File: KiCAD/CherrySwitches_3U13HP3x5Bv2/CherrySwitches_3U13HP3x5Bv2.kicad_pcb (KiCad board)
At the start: 2 copper layers, 65.7 x 128.5 mm, 19 parts

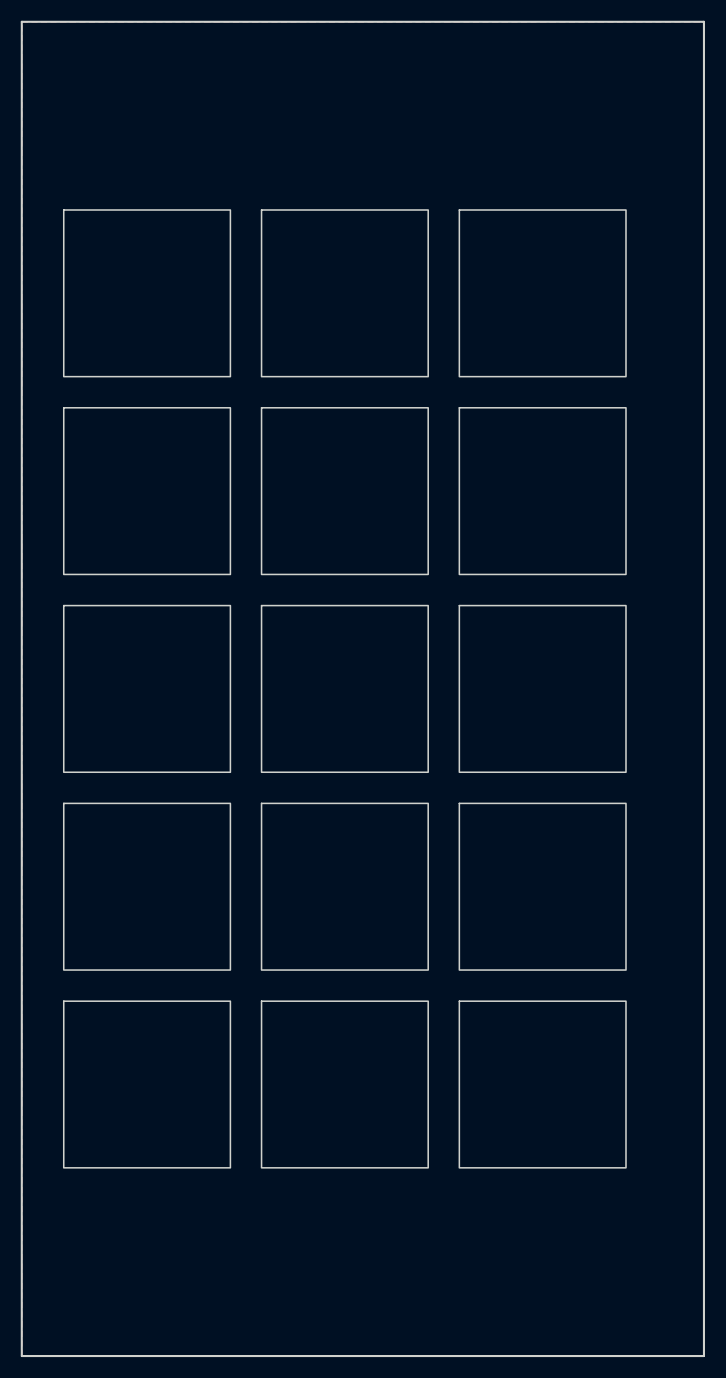
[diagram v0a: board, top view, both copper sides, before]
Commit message: updated all modules to use plated through-holes wherever possible
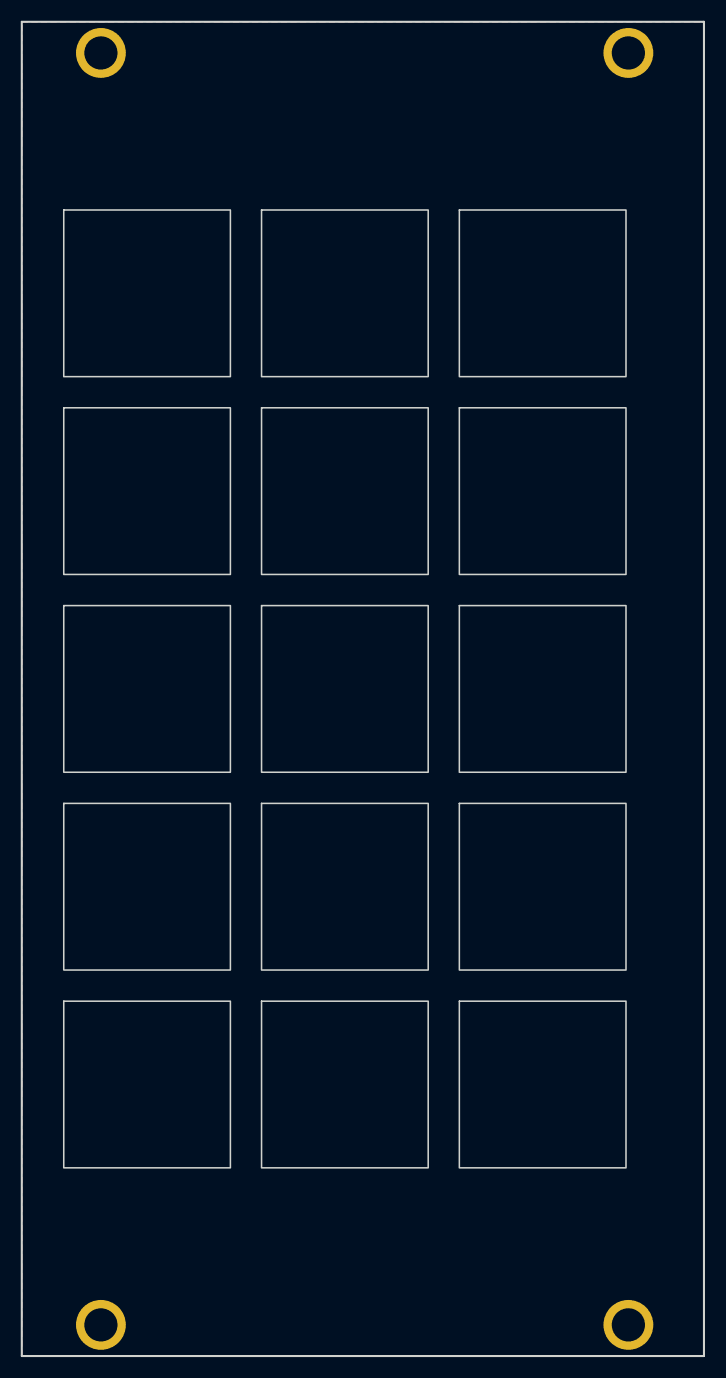
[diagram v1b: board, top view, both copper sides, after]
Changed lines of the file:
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@@
 			)
 		)
-		(pad "" np_thru_hole oval
+		(pad "" thru_hole circle
 			(at 0 0)
-			(size 4.34 3.2)
-			(drill oval 4.34 3.2)
+			(size 4.8 4.8)
+			(drill 3.2)
 			(layers "*.Cu" "*.Mask")
+			(remove_unused_layers no)
 		)
 		(embedded_fonts no)
@@
 			)
 		)
-		(pad "" np_thru_hole oval
+		(pad "" thru_hole circle
 			(at 0 0)
-			(size 4.34 3.2)
-			(drill oval 4.34 3.2)
+			(size 4.8 4.8)
+			(drill 3.2)
 			(layers "*.Cu" "*.Mask")
+			(remove_unused_layers no)
 		)
 		(embedded_fonts no)
@@
 			)
 		)
-		(pad "" np_thru_hole oval
+		(pad "" thru_hole circle
 			(at 0 0)
-			(size 4.34 3.2)
-			(drill oval 4.34 3.2)
+			(size 4.8 4.8)
+			(drill 3.2)
 			(layers "*.Cu" "*.Mask")
+			(remove_unused_layers no)
 		)
 		(embedded_fonts no)
@@
 			)
 		)
-		(pad "" np_thru_hole oval
+		(pad "" thru_hole circle
 			(at 0 0)
-			(size 4.34 3.2)
-			(drill oval 4.34 3.2)
+			(size 4.8 4.8)
+			(drill 3.2)
 			(layers "*.Cu" "*.Mask")
+			(remove_unused_layers no)
 		)
 		(embedded_fonts no)
